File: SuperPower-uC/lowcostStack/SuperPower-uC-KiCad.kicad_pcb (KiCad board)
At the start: 4 copper layers, 92.2 x 45.2 mm, 104 parts, among them J1 Battery connector, J10 External NTC, J11 DNP, J2 Thermistor, J3 USB_B_Micro, J4 Solar in, J5 Conn_01x14_Female, J6 Conn_01x14_Female, J7 DNP, J8 regulator board, J9 MCU board, Q1 2N7002, Q2 2N7002, Q3 S8050, Q4 S8050, Q5 AO3401A, Q6 AO3401A, Q7 2N7002, Q8 2N7002, Q9 AO3401A, SW1 DNP, SW2 DNP, U1 AP9101CK6-ADTRG1, U10 FP6291LR, U11 ME6210A33P, U12 ME6210A33P, U13 ESP32-WROOM32, U14 W25Q32JVSS, U2 FS8205A, U3 LC709203FQH, U4 TP4056, U5 CH340G, U6 AMS1117-3.3, U7 PCF8563T, U8 XC6206P332MR, U9 TCA6408A, Y1 12MHZ, Y2 32.768KHz

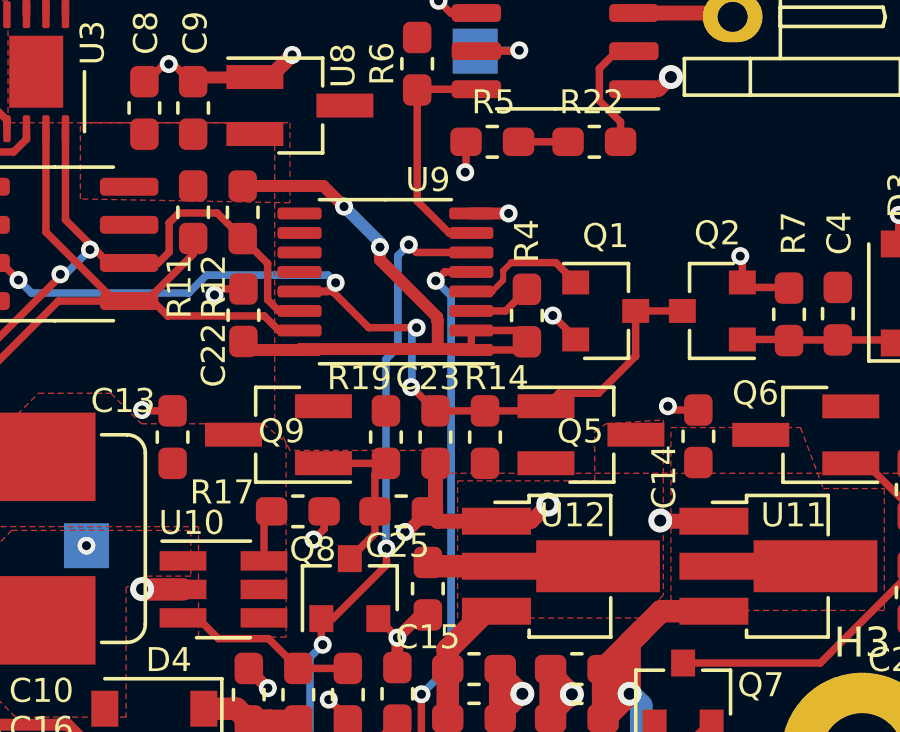
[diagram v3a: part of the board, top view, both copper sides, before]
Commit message: some more minor routing improvements
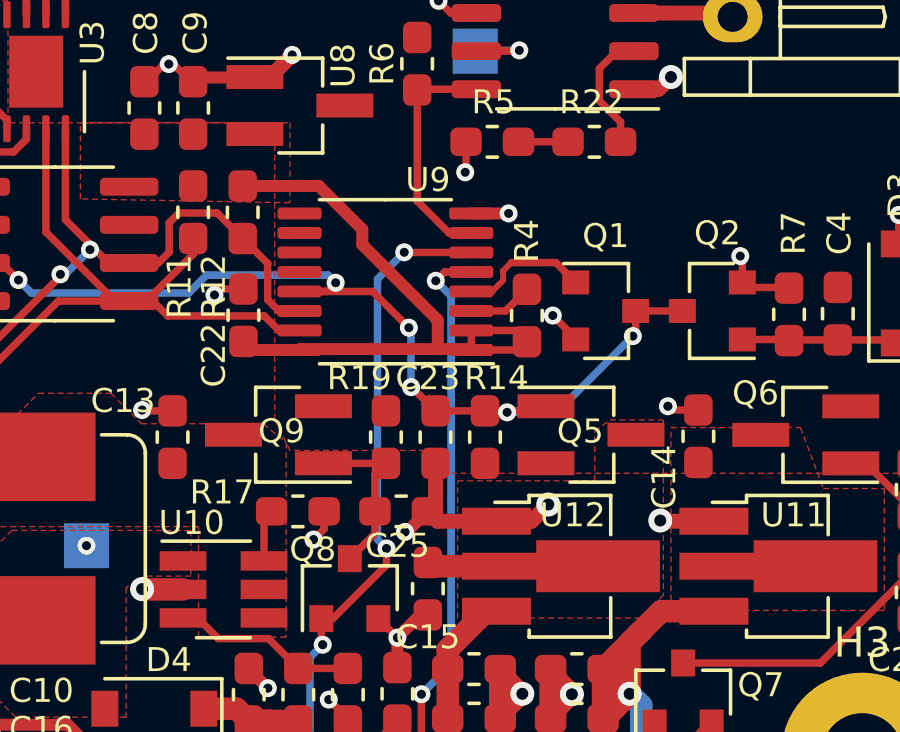
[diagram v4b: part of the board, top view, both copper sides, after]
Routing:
- net INT_IO: track 50.8 -> 51.5 mm, vias 5 -> 7
- net /Charging Module/3v3_I2C: track 22.5 -> 22.4 mm, vias 2 -> 0
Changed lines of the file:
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@@
     (thickness 1.6)
     (drawings 146)
-    (tracks 999)
+    (tracks 995)
     (zones 0)
     (modules 104)
@@
   )
   (setup
-    (last_trace_width 0.5)
+    (last_trace_width 0.25)
     (user_trace_width 0.2)
     (user_trace_width 0.4)
@@
     (trace_clearance 0.2)
     (zone_clearance 0.2)
-    (zone_45_only yes)
+    (zone_45_only no)
     (trace_min 0.2)
     (via_size 0.8)
@@
   (segment (start 179.29431 102.84889) (end 179.29431 103.166848) (width 0.2) (layer F.Cu) (net 22))
   (segment (start 179.56441 102.57879) (end 179.29431 102.84889) (width 0.2) (layer F.Cu) (net 22))
-  (segment (start 181.04959 102.57879) (end 179.56441 102.57879) (width 0.25) (layer F.Cu) (net 22))
-  (segment (start 181.7116 103.2408) (end 181.04959 102.57879) (width 0.25) (layer F.Cu) (net 22))
+  (segment (start 181.04959 102.57879) (end 181.7116 103.2408) (width 0.25) (layer F.Cu) (net 22))
+  (segment (start 179.56441 102.57879) (end 181.04959 102.57879) (width 0.25) (layer F.Cu) (net 22))
   (segment (start 117.7086 108.6612) (end 117.8306 108.7832) (width 0.25) (layer F.Cu) (net 24))
   (segment (start 115.6436 108.6612) (end 117.7086 108.6612) (width 0.25) (layer F.Cu) (net 24))
@@
   (segment (start 137.6934 111.4806) (end 137.6934 113.2612) (width 0.4) (layer F.Cu) (net 44))
   (segment (start 180.566 107.5208) (end 180.721 107.3658) (width 0.25) (layer F.Cu) (net 45))
-  (segment (start 178.689 107.5208) (end 180.566 107.5208) (width 0.25) (layer F.Cu) (net 45))
   (segment (start 183.7116 104.1908) (end 185.2676 104.1908) (width 0.25) (layer F.Cu) (net 45))
   (segment (start 177.038 107.5208) (end 178.689 107.5208) (width 0.25) (layer F.Cu) (net 45))
@@
   (segment (start 163.573625 103.594061) (end 168.810507 103.594061) (width 0.25) (layer B.Cu) (net 45))
   (segment (start 163.13912 103.159556) (end 163.573625 103.594061) (width 0.25) (layer B.Cu) (net 45))
-  (segment (start 181.1528 106.934) (end 180.721 107.3658) (width 0.25) (layer F.Cu) (net 45))
-  (segment (start 182.4736 106.934) (end 181.1528 106.934) (width 0.25) (layer F.Cu) (net 45))
-  (segment (start 183.7116 105.696) (end 182.4736 106.934) (width 0.25) (layer F.Cu) (net 45))
-  (segment (start 183.7116 104.1908) (end 183.7116 105.696) (width 0.25) (layer F.Cu) (net 45))
   (segment (start 177.038 107.5208) (end 176.248 106.7308) (width 0.25) (layer F.Cu) (net 45))
-  (segment (start 176.2252 106.7308) (end 176.2506 106.7054) (width 0.25) (layer B.Cu) (net 45))
-  (segment (start 176.2506 106.7054) (end 176.2506 104.907426) (width 0.25) (layer B.Cu) (net 45))
   (segment (start 176.248 106.7308) (end 176.2252 106.7308) (width 0.25) (layer F.Cu) (net 45))
-  (segment (start 174.816003 104.748005) (end 176.410021 104.748005) (width 0.25) (layer F.Cu) (net 45))
-  (segment (start 176.2506 104.907426) (end 176.410021 104.748005) (width 0.25) (layer B.Cu) (net 45))
   (via (at 176.2252 106.7308) (size 0.6) (drill 0.3) (layers F.Cu B.Cu) (net 45))
-  (via (at 176.410021 104.748005) (size 0.6) (drill 0.3) (layers F.Cu B.Cu) (net 45))
-  (segment (start 172.5068 103.5408) (end 173.608798 103.5408) (width 0.25) (layer F.Cu) (net 45))
-  (segment (start 173.608798 103.5408) (end 174.816003 104.748005) (width 0.25) (layer F.Cu) (net 45))
   (segment (start 160.428302 103.4415) (end 155.5496 103.4415) (width 0.25) (layer F.Cu) (net 45))
   (segment (start 161.279202 102.5906) (end 160.428302 103.4415) (width 0.25) (layer F.Cu) (net 45))
@@
   (segment (start 152.0571 103.4415) (end 155.5496 103.4415) (width 0.25) (layer B.Cu) (net 45))
   (segment (start 150.9776 102.362) (end 152.0571 103.4415) (width 0.25) (layer B.Cu) (net 45))
+  (via (at 176.150595 104.748005) (size 0.6) (drill 0.3) (layers F.Cu B.Cu) (net 45))
+  (segment (start 176.2252 106.7308) (end 176.2252 104.82261) (width 0.25) (layer B.Cu) (net 45))
+  (segment (start 176.2252 104.82261) (end 176.150595 104.748005) (width 0.25) (layer B.Cu) (net 45))
+  (segment (start 172.5068 103.5408) (end 174.94339 103.5408) (width 0.25) (layer F.Cu) (net 45))
+  (segment (start 174.94339 103.5408) (end 176.150595 104.748005) (width 0.25) (layer F.Cu) (net 45))
+  (segment (start 179.4738 107.5208) (end 179.4256 107.569) (width 0.25) (layer F.Cu) (net 45))
+  (via (at 179.4256 107.569) (size 0.6) (drill 0.3) (layers F.Cu B.Cu) (net 45))
+  (segment (start 178.689 107.5208) (end 179.4738 107.5208) (width 0.25) (layer F.Cu) (net 45))
+  (segment (start 179.4738 107.5208) (end 180.566 107.5208) (width 0.25) (layer F.Cu) (net 45))
+  (via (at 183.6166 105.029) (size 0.6) (drill 0.3) (layers F.Cu B.Cu) (net 45))
+  (segment (start 183.7116 104.934) (end 183.6166 105.029) (width 0.25) (layer F.Cu) (net 45))
+  (segment (start 183.7116 104.1908) (end 183.7116 104.934) (width 0.25) (layer F.Cu) (net 45))
+  (segment (start 181.0766 107.569) (end 179.4256 107.569) (width 0.25) (layer B.Cu) (net 45))
+  (segment (start 183.6166 105.029) (end 181.0766 107.569) (width 0.25) (layer B.Cu) (net 45))
   (segment (start 192.913 112.6998) (end 192.913 111.0208) (width 0.25) (layer F.Cu) (net 46))
   (segment (start 189.868336 115.9256) (end 185.293 115.9256) (width 0.25) (layer F.Cu) (net 46))
@@
   (segment (start 172.856999 118.481001) (end 172.856999 115.737801) (width 0.25) (layer B.Cu) (net 62))
   (segment (start 171.196 120.142) (end 172.856999 118.481001) (width 0.25) (layer B.Cu) (net 62))
-  (via (at 176.149 101.981004) (size 0.6) (drill 0.3) (layers F.Cu B.Cu) (net 62))
-  (segment (start 176.408796 102.2408) (end 176.149 101.981004) (width 0.25) (layer F.Cu) (net 62))
-  (segment (start 178.2318 102.2408) (end 176.408796 102.2408) (width 0.25) (layer F.Cu) (net 62))
-  (segment (start 175.785011 102.344993) (end 176.149 101.981004) (width 0.25) (layer B.Cu) (net 62))
-  (segment (start 175.404742 112.107942) (end 175.387 112.0902) (width 0.25) (layer B.Cu) (net 62))
-  (segment (start 175.387 105.802664) (end 175.785011 105.404653) (width 0.25) (layer B.Cu) (net 62))
-  (segment (start 175.785011 105.404653) (end 175.785011 102.344993) (width 0.25) (layer B.Cu) (net 62))
-  (segment (start 175.387 112.0902) (end 175.387 105.802664) (width 0.25) (layer B.Cu) (net 62))
+  (via (at 175.9966 102.235) (size 0.6) (drill 0.3) (layers F.Cu B.Cu) (net 62))
+  (segment (start 175.104743 103.126857) (end 175.9966 102.235) (width 0.25) (layer B.Cu) (net 62))
+  (segment (start 178.2318 102.2408) (end 176.0024 102.2408) (width 0.25) (layer F.Cu) (net 62))
+  (segment (start 176.0024 102.2408) (end 175.9966 102.235) (width 0.25) (layer F.Cu) (net 62))
+  (segment (start 175.104743 111.807943) (end 175.104743 103.126857) (width 0.25) (layer B.Cu) (net 62))
+  (segment (start 175.404742 112.107942) (end 175.104743 111.807943) (width 0.25) (layer B.Cu) (net 62))
   (via (at 124.0536 112.369608) (size 0.8) (drill 0.4) (layers F.Cu B.Cu) (net 63))
   (segment (start 124.0536 112.268) (end 125.0188 111.3028) (width 0.5) (layer F.Cu) (net 63))
@@
   (segment (start 178.2318 105.4908) (end 178.2018 105.4608) (width 0.4) (layer F.Cu) (net 108))
   (segment (start 178.2018 105.4608) (end 177.1142 105.4608) (width 0.4) (layer F.Cu) (net 108))
-  (via (at 173.99 100.711) (size 0.6) (drill 0.3) (layers F.Cu B.Cu) (net 108))
-  (segment (start 173.3042 100.0252) (end 170.6118 100.0252) (width 0.4) (layer F.Cu) (net 108))
-  (segment (start 173.99 100.711) (end 173.3042 100.0252) (width 0.4) (layer F.Cu) (net 108))
-  (segment (start 175.18696 101.90796) (end 175.18696 102.061804) (width 0.4) (layer B.Cu) (net 108))
-  (via (at 175.18696 102.061804) (size 0.6) (drill 0.3) (layers F.Cu B.Cu) (net 108))
-  (segment (start 173.99 100.711) (end 175.18696 101.90796) (width 0.4) (layer B.Cu) (net 108))
-  (segment (start 175.18696 102.486068) (end 175.18696 102.061804) (width 0.4) (layer F.Cu) (net 108))
-  (segment (start 177.1142 105.4608) (end 177.1142 104.517824) (width 0.4) (layer F.Cu) (net 108))
   (segment (start 172.5368 105.4608) (end 172.5068 105.4908) (width 0.4) (layer F.Cu) (net 108))
-  (segment (start 177.09429 104.393398) (end 175.18696 102.486068) (width 0.4) (layer F.Cu) (net 108))
   (segment (start 177.1142 105.4608) (end 172.5368 105.4608) (width 0.4) (layer F.Cu) (net 108))
-  (segment (start 177.1142 104.517824) (end 177.09429 104.497914) (width 0.4) (layer F.Cu) (net 108))
-  (segment (start 177.09429 104.497914) (end 177.09429 104.393398) (width 0.4) (layer F.Cu) (net 108))
+  (segment (start 177.1142 104.517824) (end 177.1142 105.4608) (width 0.4) (layer F.Cu) (net 108))
+  (segment (start 177.09429 104.47569) (end 177.09429 104.497914) (width 0.4) (layer F.Cu) (net 108))
+  (segment (start 174.5996 101.981) (end 177.09429 104.47569) (width 0.4) (layer F.Cu) (net 108))
+  (segment (start 174.5996 101.473) (end 174.5996 101.981) (width 0.4) (layer F.Cu) (net 108))
+  (segment (start 173.1518 100.0252) (end 174.5996 101.473) (width 0.4) (layer F.Cu) (net 108))
+  (segment (start 177.09429 104.497914) (end 177.1142 104.517824) (width 0.4) (layer F.Cu) (net 108))
+  (segment (start 170.6118 100.0252) (end 173.1518 100.0252) (width 0.4) (layer F.Cu) (net 108))
   (zone (net 2) (net_name GND) (layer B.Cu) (hatch edge 0.508)
     (connect_pads (clearance 0.2))
@@
     (connect_pads (clearance 0.2))
     (min_thickness 0.2)
-    (fill yes (arc_segments 32) (thermal_gap 0.2) (thermal_bridge_width 0.4))
+    (fill yes (arc_segments 32) (thermal_gap 0.2) (thermal_bridge_width 0.3))
     (polygon
       (pts
         (xy 184.6326 113.665) (xy 183.8706 114.427) (xy 177.7746 114.427) (xy 177.7746 109.855) (xy 182.3466 109.855)
-        (xy 182.3466 108.204) (xy 182.7276 107.95) (xy 184.6326 107.823)
+        (xy 182.3466 108.204) (xy 182.8546 107.823) (xy 184.6326 107.823)
       )
     )

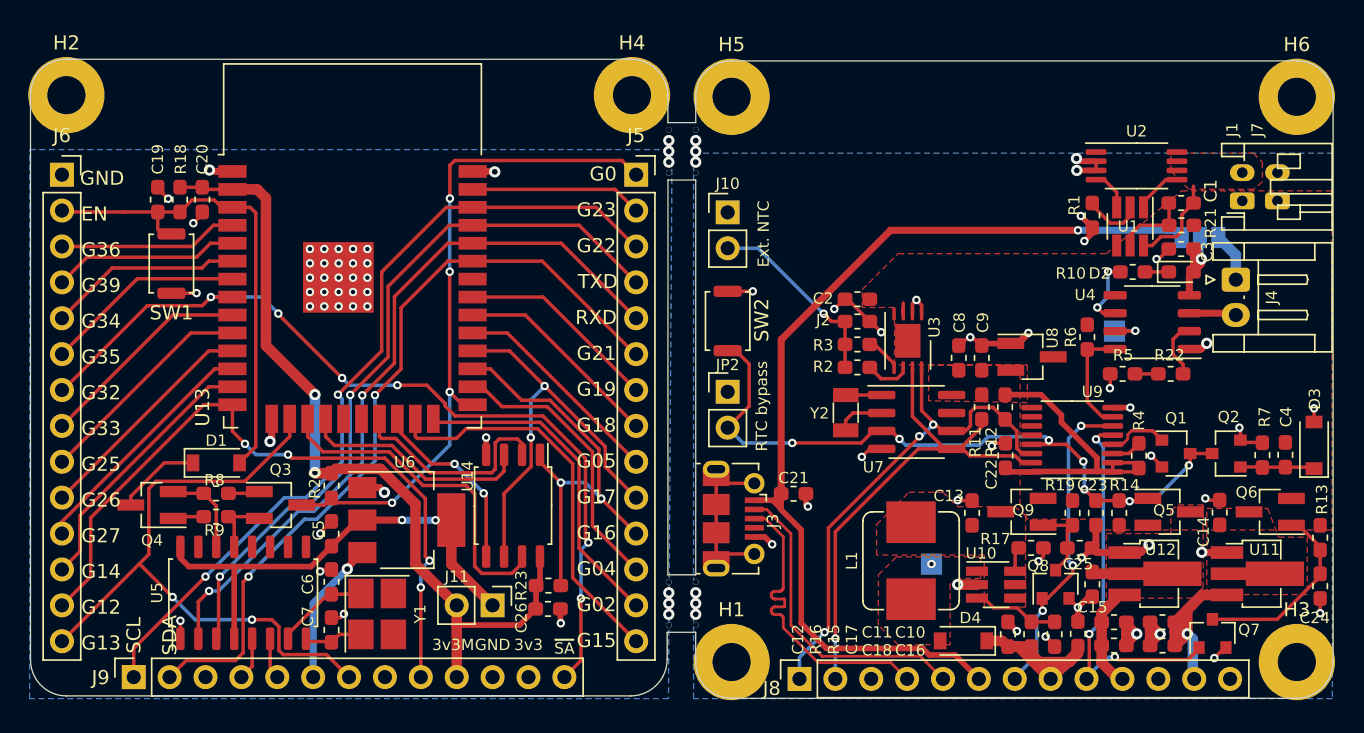
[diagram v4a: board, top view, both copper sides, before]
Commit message: added USB input ESD Proteciton ic footprint
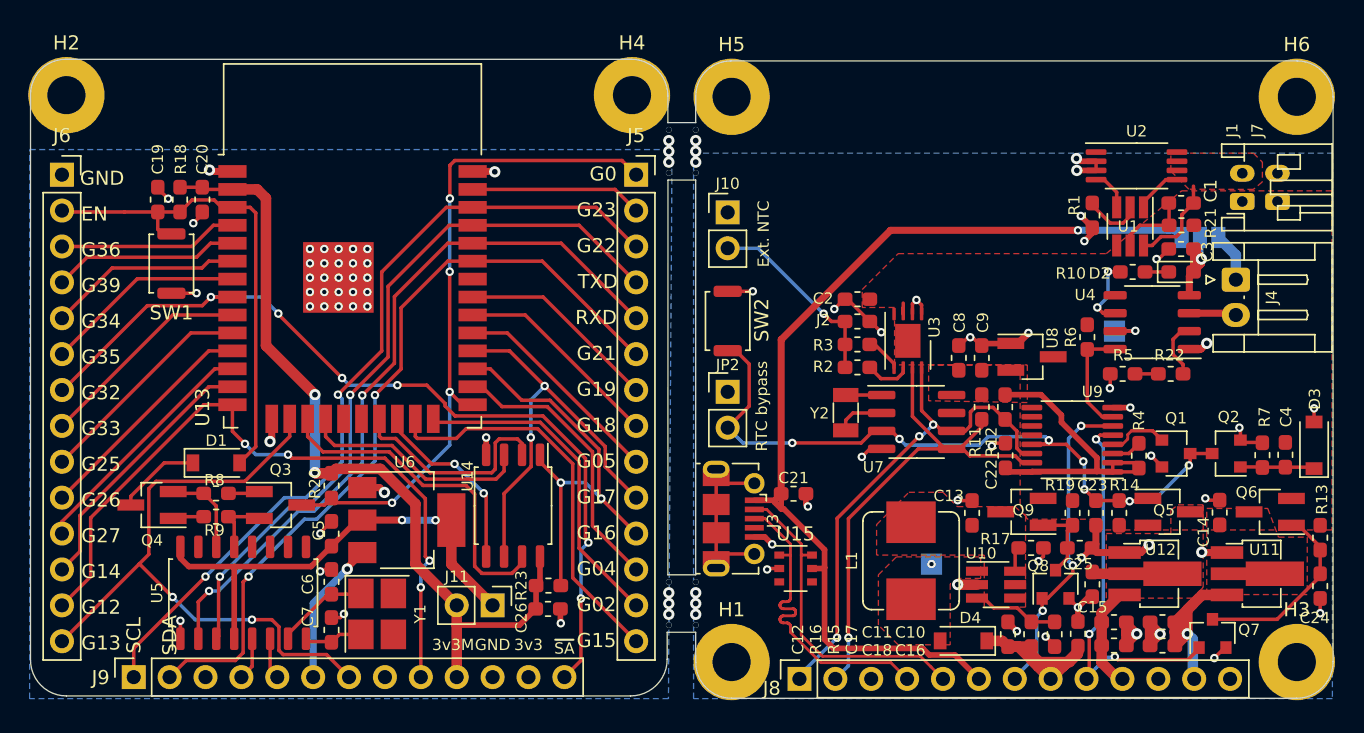
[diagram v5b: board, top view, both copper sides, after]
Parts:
- added U15: IP4220CZ6, Package_SO:TSOP-6_1.65x3.05mm_P0.95mm, F.Cu at (155.8, 112.3)
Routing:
- net GND: track 84.2 -> 85.1 mm, vias 73 -> 74
- net /D1-: track 22.1 -> 22.9 mm
- net /D1+: track 22.1 -> 22.9 mm
- net /VBUS_1: track 69.5 -> 70.2 mm

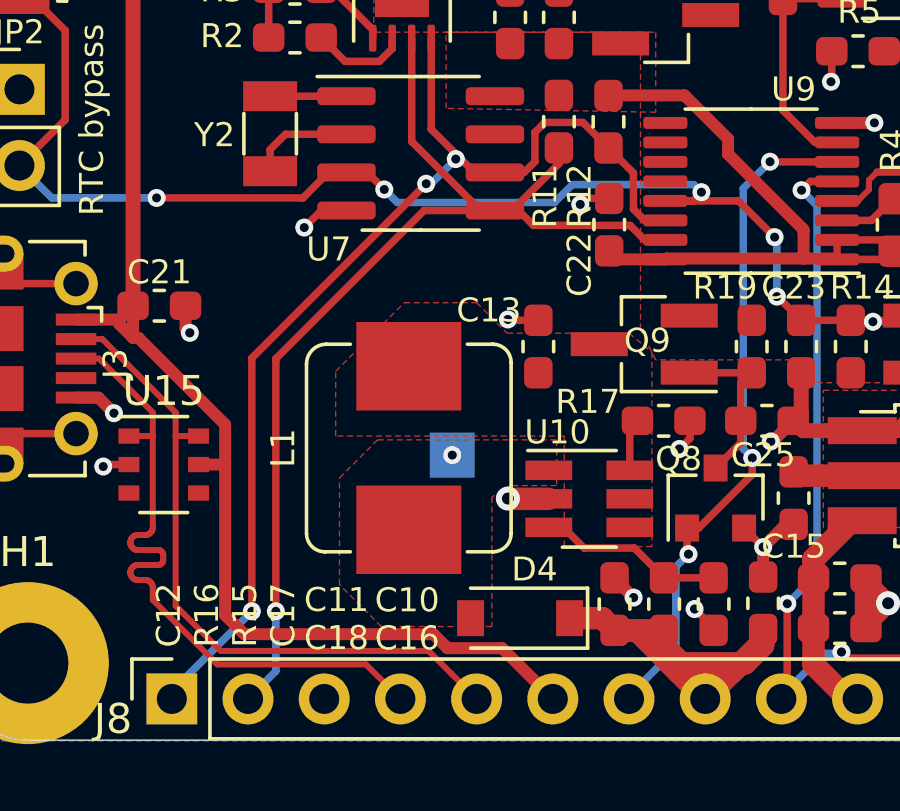
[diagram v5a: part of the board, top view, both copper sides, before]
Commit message: added missing 3d packages, added inductor gnd shield
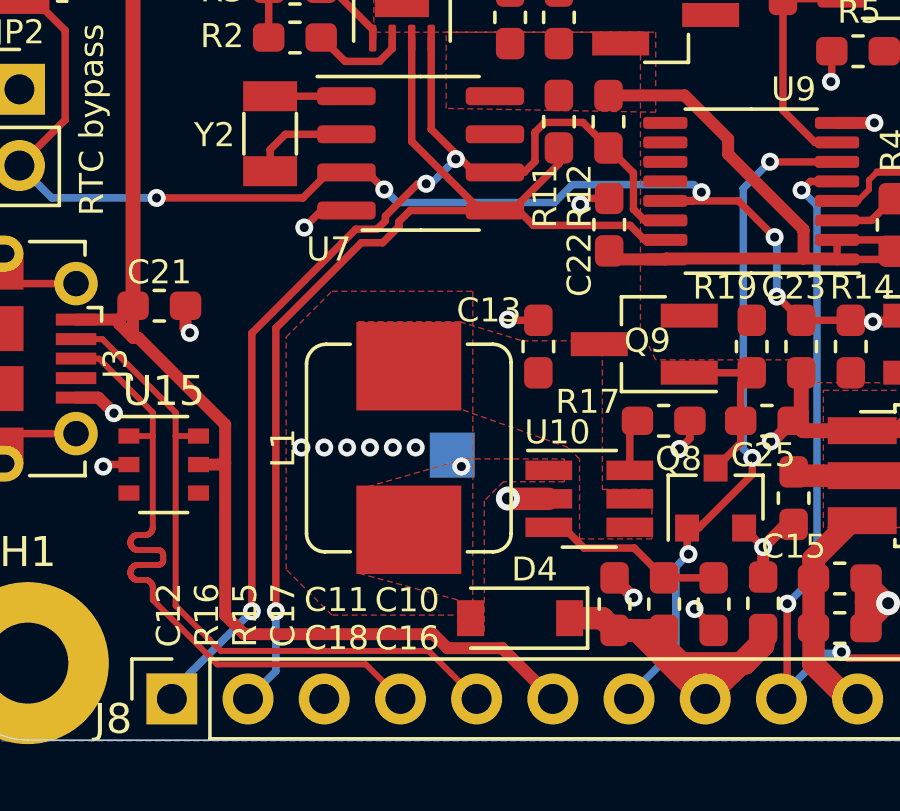
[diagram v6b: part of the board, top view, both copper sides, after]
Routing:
- net /SDA_1: track 37.6 -> 38.3 mm
- net /SCL_1: track 36.8 -> 37.4 mm
- net GND: vias 74 -> 80
- added copper zone on F.Cu, net GND
